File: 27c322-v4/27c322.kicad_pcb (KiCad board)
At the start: 2 copper layers, 47 x 86.4 mm, 10 parts, among them Q1 MMBT3906, SW1 Switch_SPDT_x2, SW2 SW_Coded_SH-7010, U1 27C4096, U2 27C322

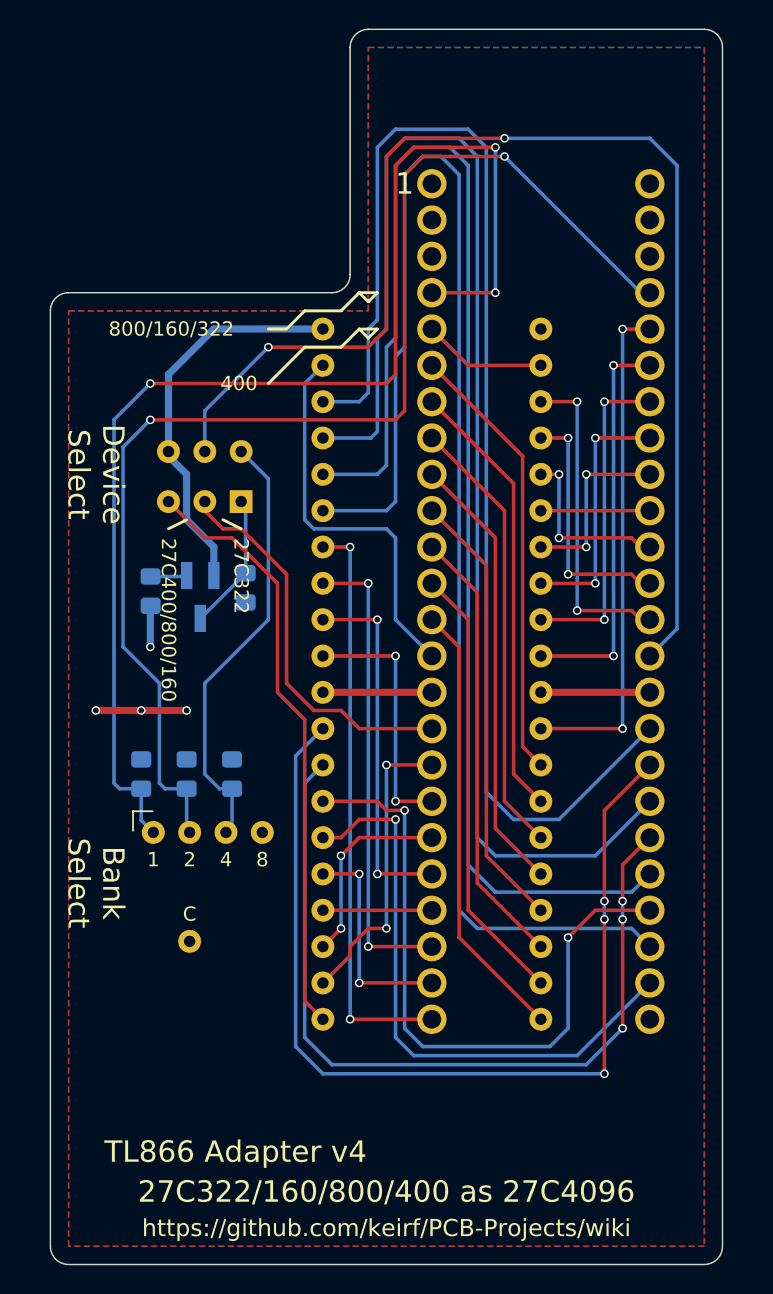
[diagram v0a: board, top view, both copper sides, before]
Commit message: changed to THT components added jumpers additionally to rotary switch
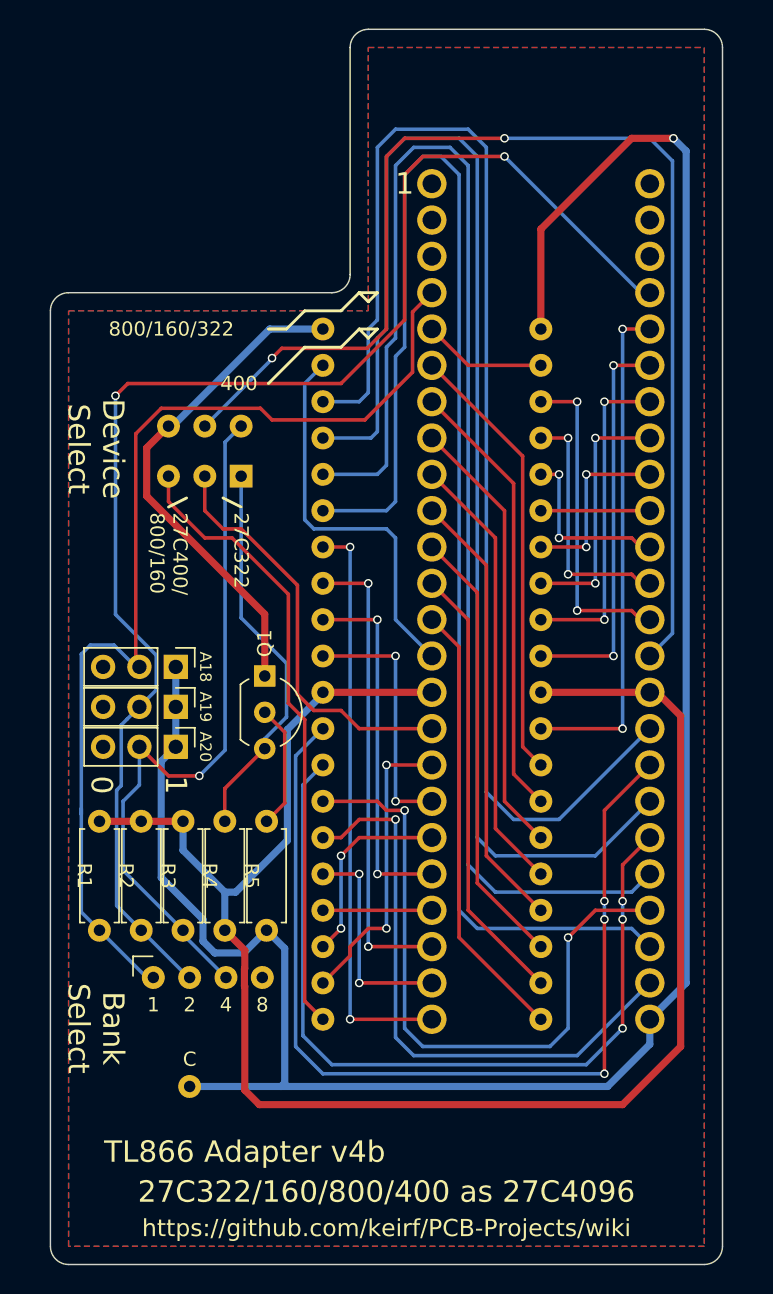
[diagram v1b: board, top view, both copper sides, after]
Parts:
- added A18: Jumper_3_Open, Connector_PinHeader_2.54mm:PinHeader_1x03_P2.54mm_Vertical, F.Cu at (123.1, 87.8)
- added A19: Jumper_3_Open, Connector_PinHeader_2.54mm:PinHeader_1x03_P2.54mm_Vertical, F.Cu at (123.1, 90.6)
- added A20: Jumper_3_Open, Connector_PinHeader_2.54mm:PinHeader_1x03_P2.54mm_Vertical, F.Cu at (123.1, 93.3)
- Q1: value MMBT3906 -> 2N3906TAR; footprint Package_TO_SOT_SMD:SOT-23_Handsoldering -> Package_TO_SOT_THT:TO-92L_Inline_Wide; moved to F.Cu
- R1, R2, R3, R4, R5: footprint Resistor_SMD:R_0805_2012Metric_Pad1.15x1.40mm_HandSolder -> Resistor_THT:R_Axial_DIN0207_L6.3mm_D2.5mm_P7.62mm_Horizontal; moved to F.Cu
- moved R5 18.0 mm to (129.4, 98.6)
- moved R4 16.4 mm to (126.5, 98.6)
- moved SW2 10.1 mm to (121.5, 109.5)
- moved Q1 7.13 mm to (129.3, 88.4)
- moved R3 4.76 mm to (123.6, 98.6)
- moved R2 4.58 mm to (120.7, 98.6)
- moved R1 4.41 mm to (117.7, 98.6)
- moved SW1 1.78 mm to (127.6, 74.4)
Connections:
- Q1 pad 1: Net-(Q1-Pad1) -> /VPP
- Q1 pad 2: /VPP -> Net-(Q1-Pad2)
- R5 pad 1: Net-(Q1-Pad1) -> Net-(Q1-Pad2)
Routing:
- net /VCC: track 2.91 -> 154.9 mm
- net /VSS: track 21.6 -> 117.5 mm, vias 3 -> 0
- net /A20: track 30.7 -> 50.6 mm, vias 0 -> 1
- net Net-(Q1-Pad3): track 9.62 -> 27.2 mm
- net /A18: track 88.6 -> 74.6 mm, vias 3 -> 0
- net /A19: track 88.6 -> 99.3 mm
- net Net-(Q1-Pad2): track 0.00 -> 8.72 mm
- net /VPP: track 27.5 -> 35.1 mm
- net Net-(SW1-Pad5): track 86.7 -> 84.1 mm
- net Net-(Q1-Pad1): track 2.55 -> 0.00 mm
- net /P20: track 41.8 -> 43.6 mm
- net Net-(SW1-Pad2): track 27.3 -> 29.1 mm
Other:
- board text added: "0"
- board text added: "27C400/ 800/160"
- board text added: "TL866 Adapter v4b"
- board text removed: "1k"
- board text removed: "27C400/800/160"
- board text removed: "TL866 Adapter v4"

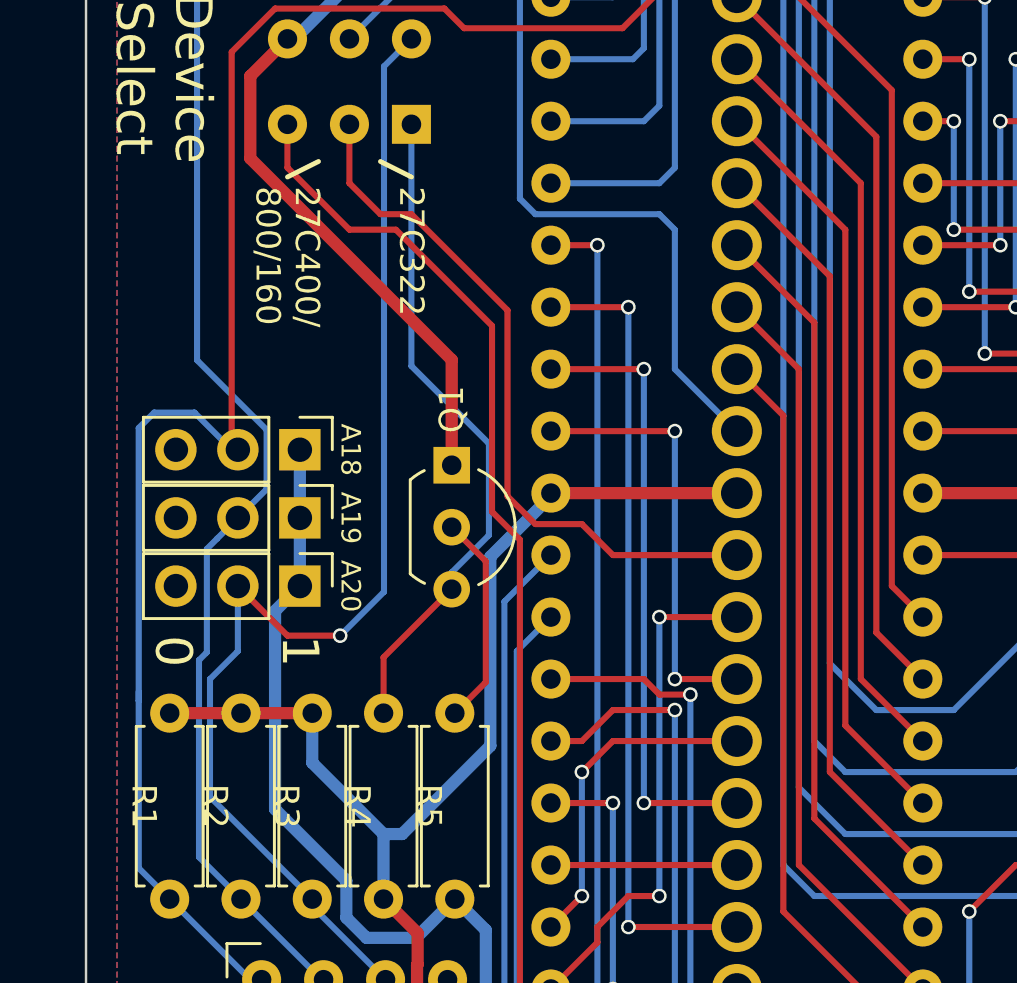
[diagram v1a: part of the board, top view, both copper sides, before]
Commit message: moved Q1 and R1 to R5 silk added JLCPCB tag
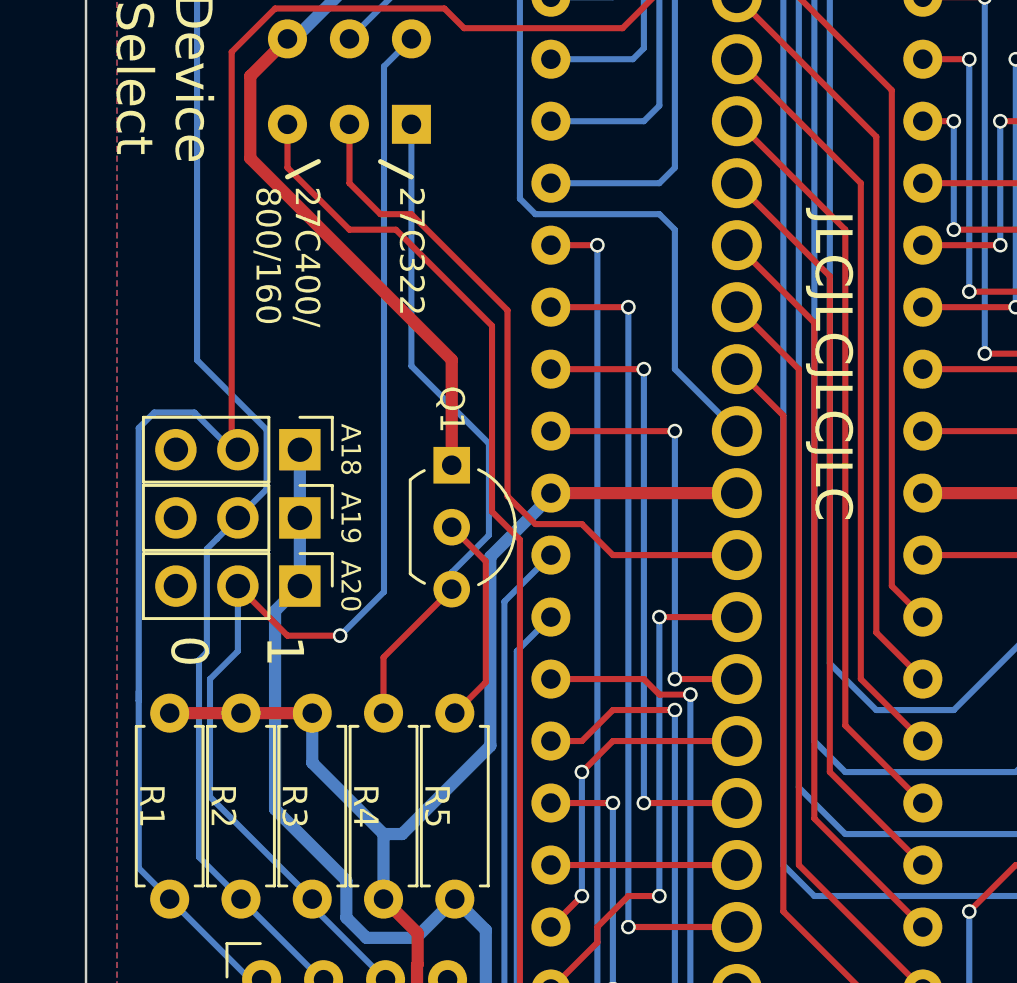
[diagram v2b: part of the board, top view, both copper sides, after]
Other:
- board text added: "JLCJLCJLCJLC"
